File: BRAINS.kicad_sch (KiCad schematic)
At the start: 2 parts

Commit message: added decoupling capacitors, perhaps too many? idk better more than less!
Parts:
- added C?: (no value), symbol Device:C_Small
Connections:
- net +5V: now also C?.1
- net GNDD: now also C?.2
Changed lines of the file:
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@@
+    (pin "1")
+  )
+  (symbol (lib_id "power:GNDD") (at 133.35 100.33 0) (unit 1)
+    (in_bom yes) (on_board yes) (fields_autoplaced)
+    (property "Reference" "#PWR?" (id 0) (at 133.35 106.68 0)
+      (effects (font (size 1.27 1.27)) hide)
+    )
+    (property "Value" "" (id 1) (at 133.35 104.775 0))
+    (property "Footprint" "" (id 2) (at 133.35 100.33 0)
+      (effects (font (size 1.27 1.27)) hide)
+    )
+    (property "Datasheet" "" (id 3) (at 133.35 100.33 0)
+      (effects (font (size 1.27 1.27)) hide)
+    )
     (pin "1")
   )
@@
     (pin "9")
   )
+  (symbol (lib_id "Device:C_Small") (at 133.35 97.79 0) (unit 1)
+    (in_bom yes) (on_board yes) (fields_autoplaced)
+    (property "Reference" "C?" (id 0) (at 135.89 96.5262 0)
+      (effects (font (size 1.27 1.27)) (justify left))
+    )
+    (property "Value" "" (id 1) (at 135.89 99.0662 0)
+      (effects (font (size 1.27 1.27)) (justify left))
+    )
+    (property "Footprint" "" (id 2) (at 133.35 97.79 0)
+      (effects (font (size 1.27 1.27)) hide)
+    )
+    (property "Datasheet" "~" (id 3) (at 133.35 97.79 0)
+      (effects (font (size 1.27 1.27)) hide)
+    )
+    (pin "1")
+    (pin "2")
+  )
+  (symbol (lib_id "power:+5V") (at 133.35 95.25 0) (unit 1)
+    (in_bom yes) (on_board yes) (fields_autoplaced)
+    (property "Reference" "#PWR?" (id 0) (at 133.35 99.06 0)
+      (effects (font (size 1.27 1.27)) hide)
+    )
+    (property "Value" "" (id 1) (at 133.35 89.535 0))
+    (property "Footprint" "" (id 2) (at 133.35 95.25 0)
+      (effects (font (size 1.27 1.27)) hide)
+    )
+    (property "Datasheet" "" (id 3) (at 133.35 95.25 0)
+      (effects (font (size 1.27 1.27)) hide)
+    )
+    (pin "1")
+  )
   (symbol (lib_id "power:+5V") (at 38.1 86.36 90) (unit 1)

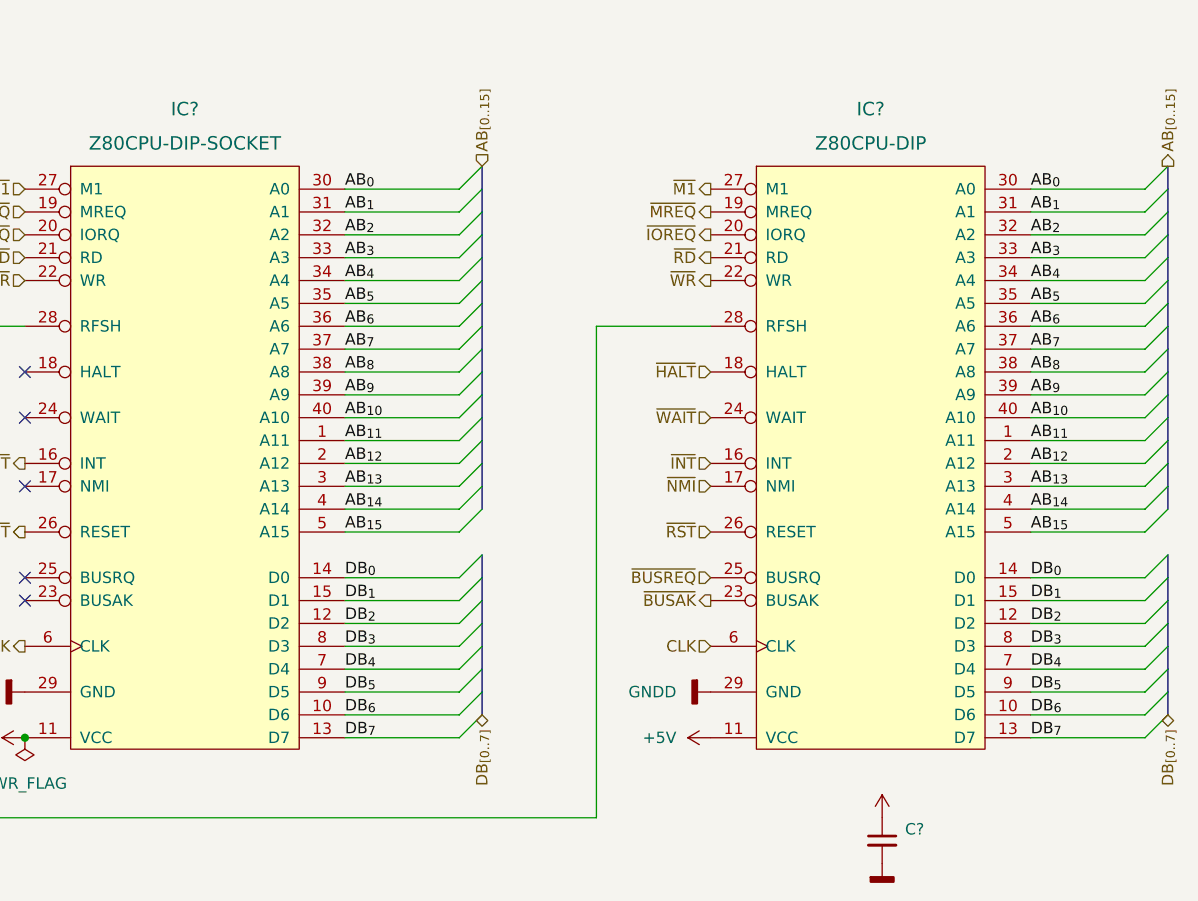
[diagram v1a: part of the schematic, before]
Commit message: some clean up and simplification, as well as some renaming
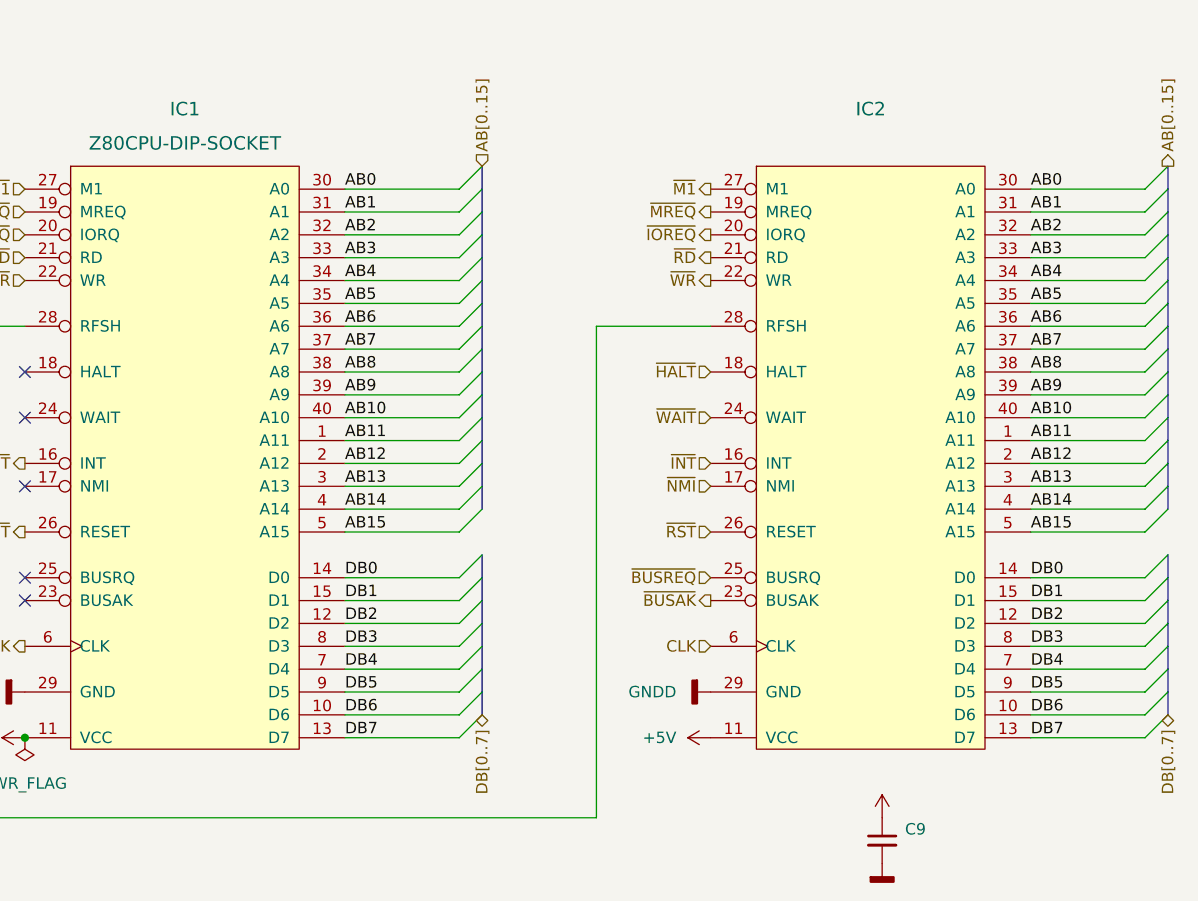
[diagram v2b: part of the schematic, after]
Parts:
- IC1: renamed from IC?; footprint Zilog Z80 Microprocessor 8bit CISC 40-Pin PDIP -> (none)
- IC2: renamed from IC?; value Z80CPU-DIP -> (none); footprint Zilog Z80 Microprocessor 8bit CISC 40-Pin PDIP -> (none)
- gave numbers to parts that had none: 1
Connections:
- net AB_{0} renamed AB0
- net AB_{10} renamed AB10
- net AB_{11} renamed AB11
- net AB_{12} renamed AB12
- net AB_{13} renamed AB13
- net AB_{14} renamed AB14
- net AB_{15} renamed AB15
- net AB_{1} renamed AB1
- net AB_{2} renamed AB2
- net AB_{3} renamed AB3
- net AB_{4} renamed AB4
- net AB_{5} renamed AB5
- net AB_{6} renamed AB6
- net AB_{7} renamed AB7
- net AB_{8} renamed AB8
- net AB_{9} renamed AB9
- net DB_{0} renamed DB0
- net DB_{1} renamed DB1
- net DB_{2} renamed DB2
- net DB_{3} renamed DB3
- net DB_{4} renamed DB4
- net DB_{5} renamed DB5
- net DB_{6} renamed DB6
- net DB_{7} renamed DB7

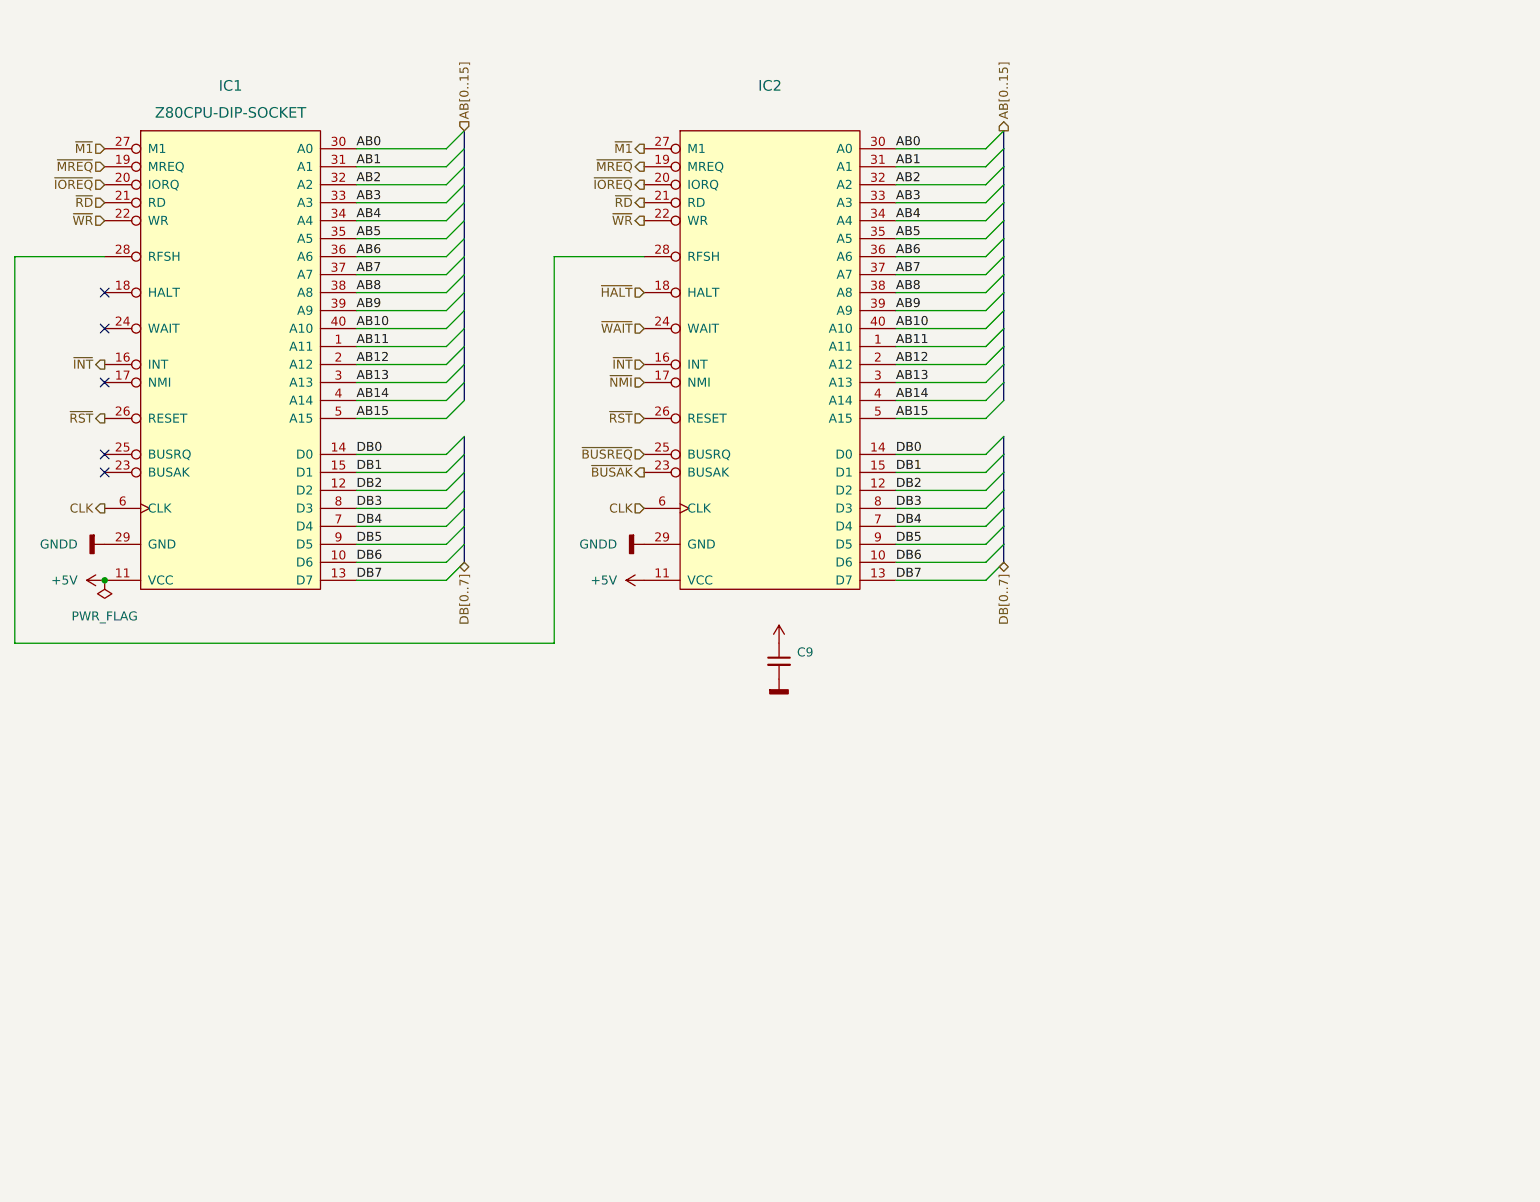
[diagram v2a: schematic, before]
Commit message: begin integration of logic into atf1508
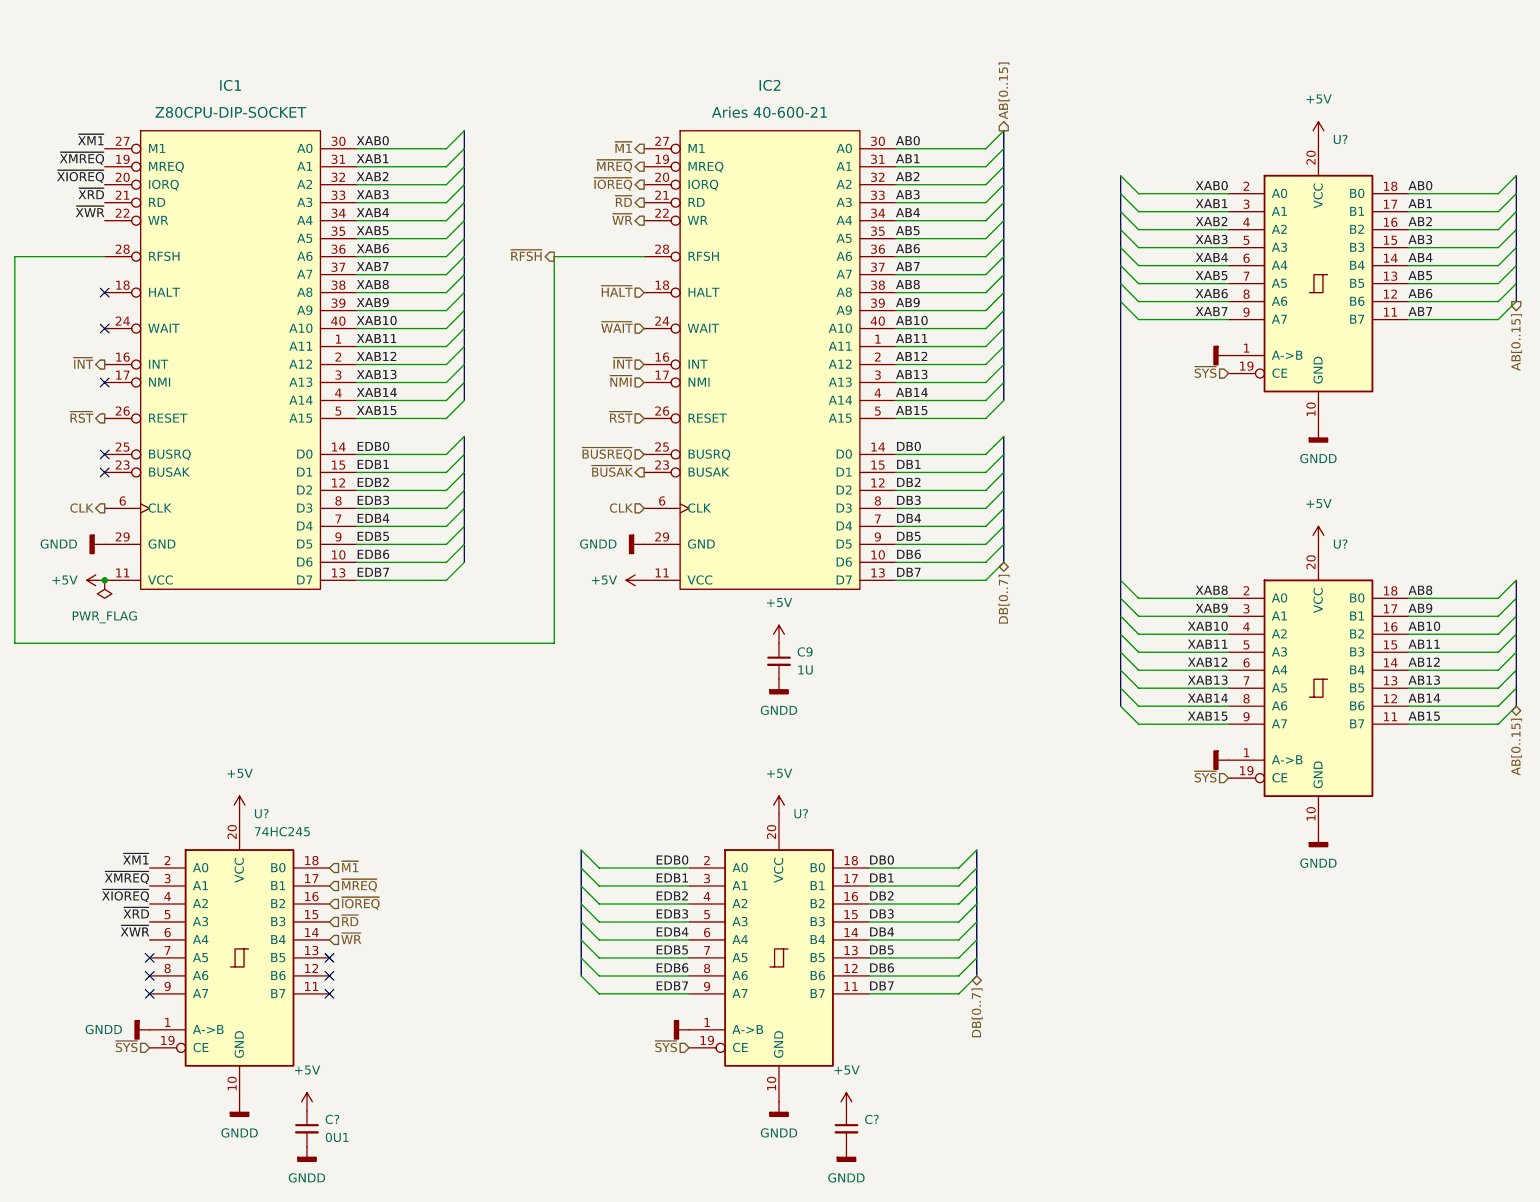
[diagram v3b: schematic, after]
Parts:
- added C?: (no value), symbol Device:C_Small
- added C?: 0U1, Capacitor_SMD:C_1206_3216Metric, symbol Device:C_Small
- added U? (x3): (no value), symbol 74xx:74HC245
- added U?: 74HC245, symbol 74xx:74HC245
- C9: value (none) -> 1U; footprint (none) -> Capacitor_SMD:C_1206_3216Metric
- IC1: footprint (none) -> Package_DIP:DIP-40_W15.24mm_Socket
- IC2: value (none) -> Aries 40-600-21; footprint (none) -> Package_DIP:DIP-40_W15.24mm_Socket
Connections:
- net +5V: now also C?.1, C?.1, U?.20 (VCC), U?.20 (VCC), U?.20 (VCC), U?.20 (VCC)
- net AB0: now also U?.18 (B0); no longer IC1.30 (A0)
- net AB1: now also U?.17 (B1); no longer IC1.31 (A1)
- net AB10: now also U?.16 (B2); no longer IC1.40 (A10)
- net AB11: now also U?.15 (B3); no longer IC1.1 (A11)
- net AB12: now also U?.14 (B4); no longer IC1.2 (A12)
- net AB13: now also U?.13 (B5); no longer IC1.3 (A13)
- net AB14: now also U?.12 (B6); no longer IC1.4 (A14)
- net AB15: now also U?.11 (B7); no longer IC1.5 (A15)
- net AB2: now also U?.16 (B2); no longer IC1.32 (A2)
- net AB3: now also U?.15 (B3); no longer IC1.33 (A3)
- net AB4: now also U?.14 (B4); no longer IC1.34 (A4)
- net AB5: now also U?.13 (B5); no longer IC1.35 (A5)
- net AB6: now also U?.12 (B6); no longer IC1.36 (A6)
- net AB7: now also U?.11 (B7); no longer IC1.37 (A7)
- net AB8: now also U?.18 (B0); no longer IC1.38 (A8)
- net AB9: now also U?.17 (B1); no longer IC1.39 (A9)
- net DB0: now also U?.18 (B0); no longer IC1.14 (D0)
- net DB1: now also U?.17 (B1); no longer IC1.15 (D1)
- net DB2: now also U?.16 (B2); no longer IC1.12 (D2)
- net DB3: now also U?.15 (B3); no longer IC1.8 (D3)
- net DB4: now also U?.14 (B4); no longer IC1.7 (D4)
- net DB5: now also U?.13 (B5); no longer IC1.9 (D5)
- net DB6: now also U?.12 (B6); no longer IC1.10 (D6)
- net DB7: now also U?.11 (B7); no longer IC1.13 (D7)
- net GNDD: now also C?.2, C?.2, U?.1 (A->B), U?.1 (A->B), U?.1 (A->B), U?.1 (A->B), U?.10 (GND), U?.10 (GND), U?.10 (GND), U?.10 (GND)
- net ~{IOREQ}: now also U?.16 (B2); no longer IC1.20 (IORQ)
- net ~{M1}: now also U?.18 (B0); no longer IC1.27 (M1)
- net ~{MREQ}: now also U?.17 (B1); no longer IC1.19 (MREQ)
- net ~{RD}: now also U?.15 (B3); no longer IC1.21 (RD)
- net ~{WR}: now also U?.14 (B4); no longer IC1.22 (WR)
- net ~{RFSH}: now reaches IC1.28 (RFSH), IC2.28 (RFSH)
- new net EDB0: IC1.14 (D0), U?.2 (A0)
- new net EDB1: IC1.15 (D1), U?.3 (A1)
- new net EDB2: IC1.12 (D2), U?.4 (A2)
- new net EDB3: IC1.8 (D3), U?.5 (A3)
- new net EDB4: IC1.7 (D4), U?.6 (A4)
- new net EDB5: IC1.9 (D5), U?.7 (A5)
- new net EDB6: IC1.10 (D6), U?.8 (A6)
- new net EDB7: IC1.13 (D7), U?.9 (A7)
- new net XAB0: IC1.30 (A0), U?.2 (A0)
- new net XAB1: IC1.31 (A1), U?.3 (A1)
- new net XAB10: IC1.40 (A10), U?.4 (A2)
- new net XAB11: IC1.1 (A11), U?.5 (A3)
- new net XAB12: IC1.2 (A12), U?.6 (A4)
- new net XAB13: IC1.3 (A13), U?.7 (A5)
- new net XAB14: IC1.4 (A14), U?.8 (A6)
- new net XAB15: IC1.5 (A15), U?.9 (A7)
- new net XAB2: IC1.32 (A2), U?.4 (A2)
- new net XAB3: IC1.33 (A3), U?.5 (A3)
- new net XAB4: IC1.34 (A4), U?.6 (A4)
- new net XAB5: IC1.35 (A5), U?.7 (A5)
- new net XAB6: IC1.36 (A6), U?.8 (A6)
- new net XAB7: IC1.37 (A7), U?.9 (A7)
- new net XAB8: IC1.38 (A8), U?.2 (A0)
- new net XAB9: IC1.39 (A9), U?.3 (A1)
- new net ~{SYS}: U?.19 (CE), U?.19 (CE), U?.19 (CE), U?.19 (CE)
- new net ~{XIOREQ}: IC1.20 (IORQ), U?.4 (A2)
- new net ~{XM1}: IC1.27 (M1), U?.2 (A0)
- new net ~{XMREQ}: IC1.19 (MREQ), U?.3 (A1)
- new net ~{XRD}: IC1.21 (RD), U?.5 (A3)
- new net ~{XWR}: IC1.22 (WR), U?.6 (A4)
- no-connect marks 5 -> 11

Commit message: added ATF150x part (specifically the 1508) vhdl file contains the (hopeful) implementition of the mapper
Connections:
- net ~{HALT}: now also IC1.18 (HALT)
- net ~{SYS}: no longer U?.19 (CE), U?.19 (CE)
- net ~{WAIT}: now also IC1.24 (WAIT)
- no-connect marks 11 -> 9
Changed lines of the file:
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@@
   (junction (at 38.1 86.36) (diameter 0) (color 0 0 0 0)
   )
-  (no_connect (at 38.1 50.8))
-  (no_connect (at 38.1 45.72))
   (no_connect (at 44.45 139.7))
   (no_connect (at 69.85 144.78))
@@
     (effects (font (size 1.27 1.27)) (justify left bottom))
   )
+  (label "~{HALT}" (at 114.3 45.72 180)
+    (effects (font (size 1.27 1.27)) (justify right bottom))
+  )
   (label "AB2" (at 149.86 30.48 0)
     (effects (font (size 1.27 1.27)) (justify left bottom))
@@
     (effects (font (size 1.27 1.27)) (justify left bottom))
   )
+  (label "~{WAIT}" (at 114.3 50.8 180)
+    (effects (font (size 1.27 1.27)) (justify right bottom))
+  )
+  (label "~{WAIT}" (at 38.1 50.8 180)
+    (effects (font (size 1.27 1.27)) (justify right bottom))
+  )
   (label "AB4" (at 149.86 35.56 0)
     (effects (font (size 1.27 1.27)) (justify left bottom))
@@
   (label "AB12" (at 222.25 99.06 0)
     (effects (font (size 1.27 1.27)) (justify left bottom))
+  )
+  (label "~{HALT}" (at 38.1 45.72 180)
+    (effects (font (size 1.27 1.27)) (justify right bottom))
   )
   (label "XAB2" (at 196.85 36.83 180)
@@
     (effects (font (size 1.27 1.27)) (justify left))
   )
-  (hierarchical_label "~{HALT}" (shape input) (at 114.3 45.72 180)
-    (effects (font (size 1.27 1.27)) (justify right))
-  )
   (hierarchical_label "~{SYS}" (shape input) (at 196.85 57.15 180)
     (effects (font (size 1.27 1.27)) (justify right))
@@
     (effects (font (size 1.27 1.27)) (justify right))
   )
-  (hierarchical_label "~{WAIT}" (shape input) (at 114.3 50.8 180)
-    (effects (font (size 1.27 1.27)) (justify right))
-  )
   (hierarchical_label "~{MREQ}" (shape input) (at 69.85 129.54 0)
     (effects (font (size 1.27 1.27)) (justify left))
   )
-  (hierarchical_label "~{SYS}" (shape input) (at 120.65 152.4 180)
-    (effects (font (size 1.27 1.27)) (justify right))
-  )
   (hierarchical_label "~{M1}" (shape output) (at 114.3 25.4 180)
     (effects (font (size 1.27 1.27)) (justify right))
@@
     (effects (font (size 1.27 1.27)) (justify right))
   )
-  (hierarchical_label "~{SYS}" (shape input) (at 44.45 152.4 180)
-    (effects (font (size 1.27 1.27)) (justify right))
-  )
